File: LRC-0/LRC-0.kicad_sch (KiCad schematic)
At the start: 39 parts, among them J1 USB_C_Receptacle_USB2.0_14P, J2 Battery, SW1 SW_Push, SW2 SW_Push, U1 ESP32-C6-MINI-1, U2 SX1262IMLTRT, U3 TVS1400DRV, U4 NCP1117-3.3_SOT223, U5 TP4056-42-ESOP8, U6 BQ24075RGT

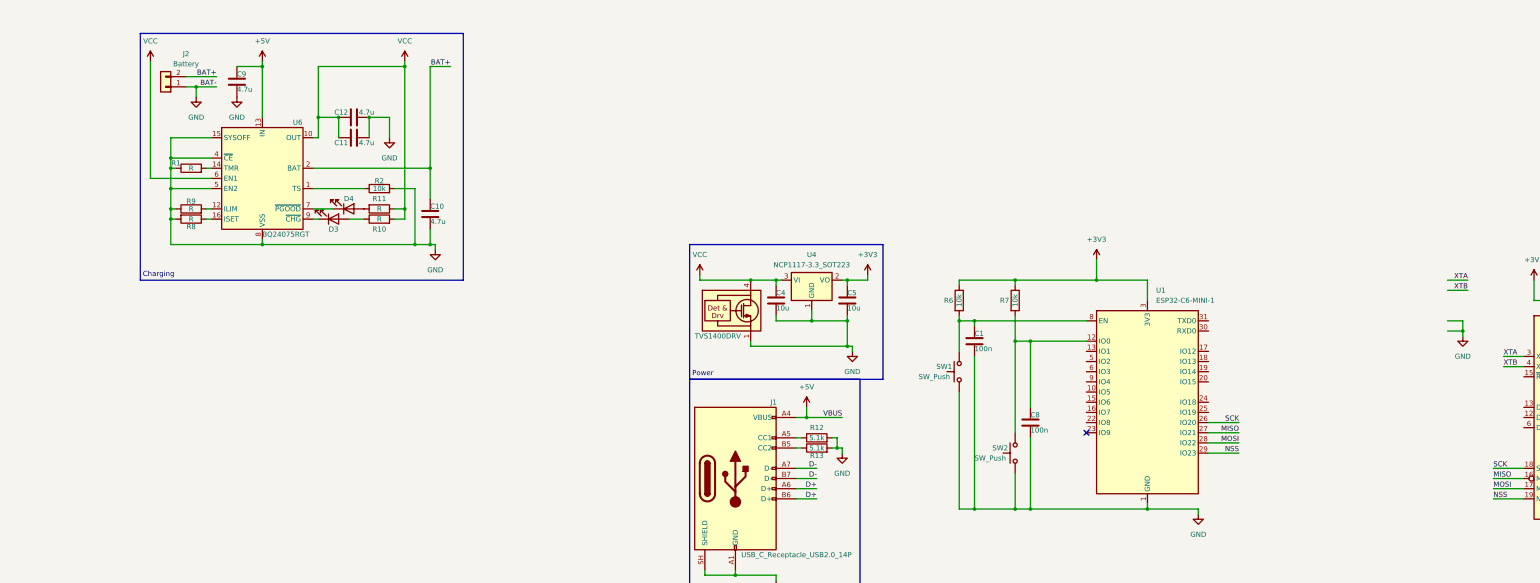
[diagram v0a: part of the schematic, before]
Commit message: footprints fixed for real
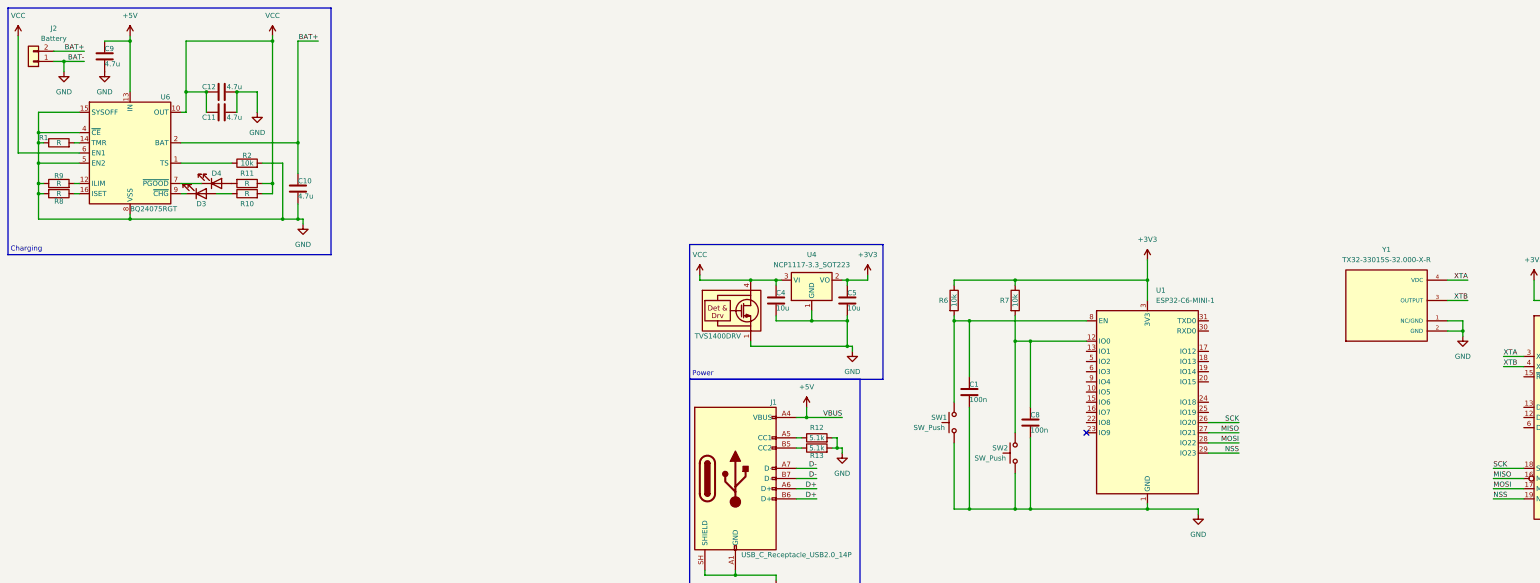
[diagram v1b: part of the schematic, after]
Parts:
- added Y1: TX32-33015S-32.000-X-R, TX32_33015S_32_000_X_R:OSC_TX32-33015S-32.000-X-R, symbol TX32_33015S_32_000_X_R:TX32-33015S-32.000-X-R
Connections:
- net GND: now also Y1.1 (NC/GND), Y1.2 (GND)
- net XTA: now also Y1.4 (VDC)
- net XTB: now also Y1.3 (OUTPUT)
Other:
- moved on the sheet: C1, C10, C11, C12, C9, D3, D4, J2, R1, R10, R11, R2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

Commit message: library dependencies fixed
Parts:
- U1: footprint RF_Module:XCVR_ESP32-C6-MINI-1U-H4 -> ESP32_C6_MINI_1U_H4:XCVR_ESP32-C6-MINI-1U-H4
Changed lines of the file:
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@@
 			)
 		)
-		(property "Footprint" "RF_Module:XCVR_ESP32-C6-MINI-1U-H4"
+		(property "Footprint" "ESP32_C6_MINI_1U_H4:XCVR_ESP32-C6-MINI-1U-H4"
 			(at 144.78 124.46 0)
 			(hide yes)

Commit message: xta fix
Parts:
- added C6: 10p, symbol Device:C
- added C7: 100n, symbol Device:C
- added L1: L, symbol Device:L
- added R14: 220, symbol Device:R
- U1: footprint ESP32_C6_MINI_1U_H4:XCVR_ESP32-C6-MINI-1U-H4 -> RF_Module:ESP32-C6-MINI-1
- Y1: footprint TX32_33015S_32_000_X_R:OSC_TX32-33015S-32.000-X-R -> TX32-33015S-32.000-X-R:OSC_TX32-33015S-32.000-X-R
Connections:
- net GND: now also C7.2
- net RFO: now also L1.1
- net XTA: now also R14.1; no longer U2.3 (XTA)
- net DIO3: now reaches U2.6 (DIO3)
- net DIO3: now also Y1.3 (OUTPUT), C7.1
- net XTB: no longer names the net of U2.4 (XTB)
- net XTB: no longer Y1.3 (OUTPUT)
- new net: C6.1, R14.2
- new net: C6.2, U2.3 (XTA)
- no-connect marks 1 -> 2
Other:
- moved on the sheet: C2, C4, C5, D1, D2, J1, R12, R13, R4, R5, U4, Y1

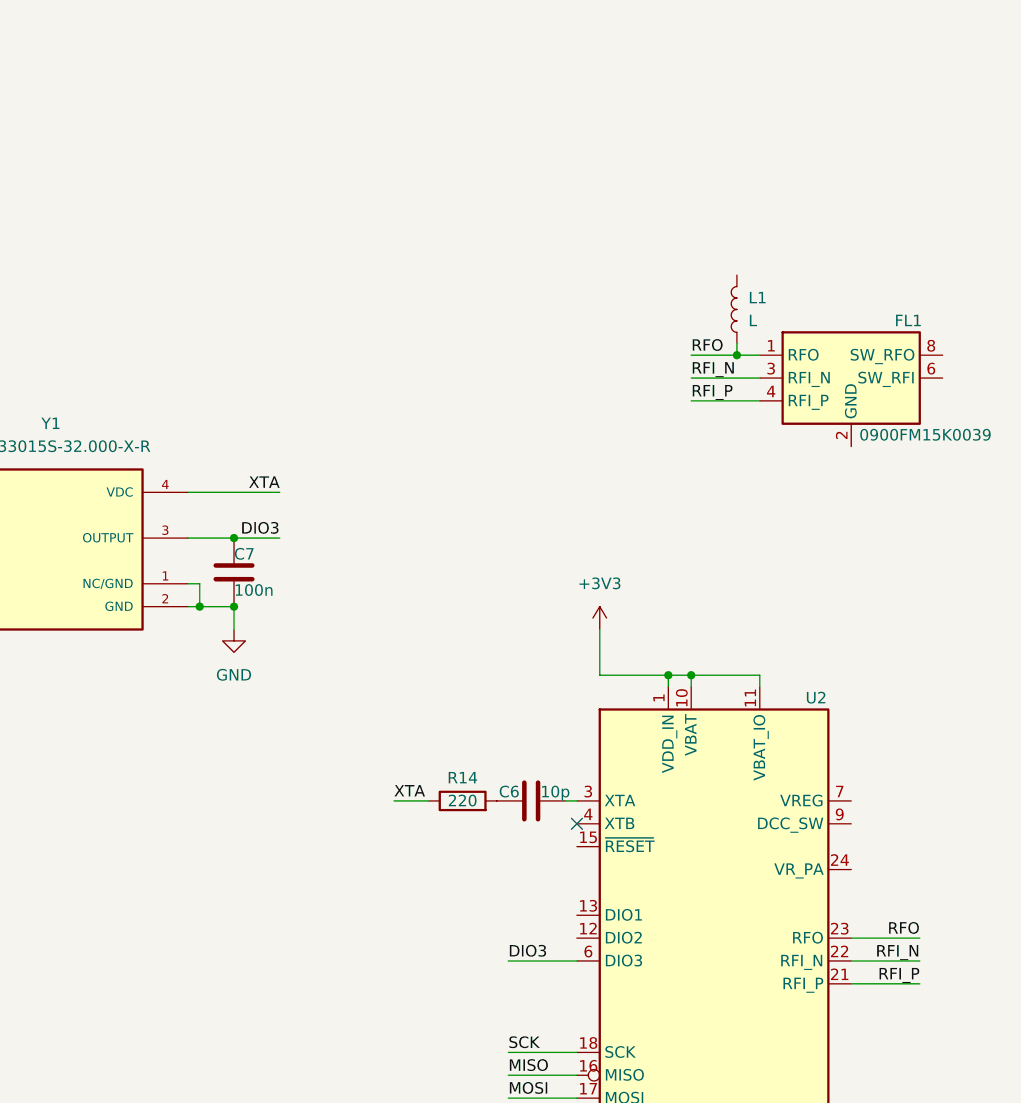
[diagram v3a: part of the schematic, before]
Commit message: schematic progress new rf switch
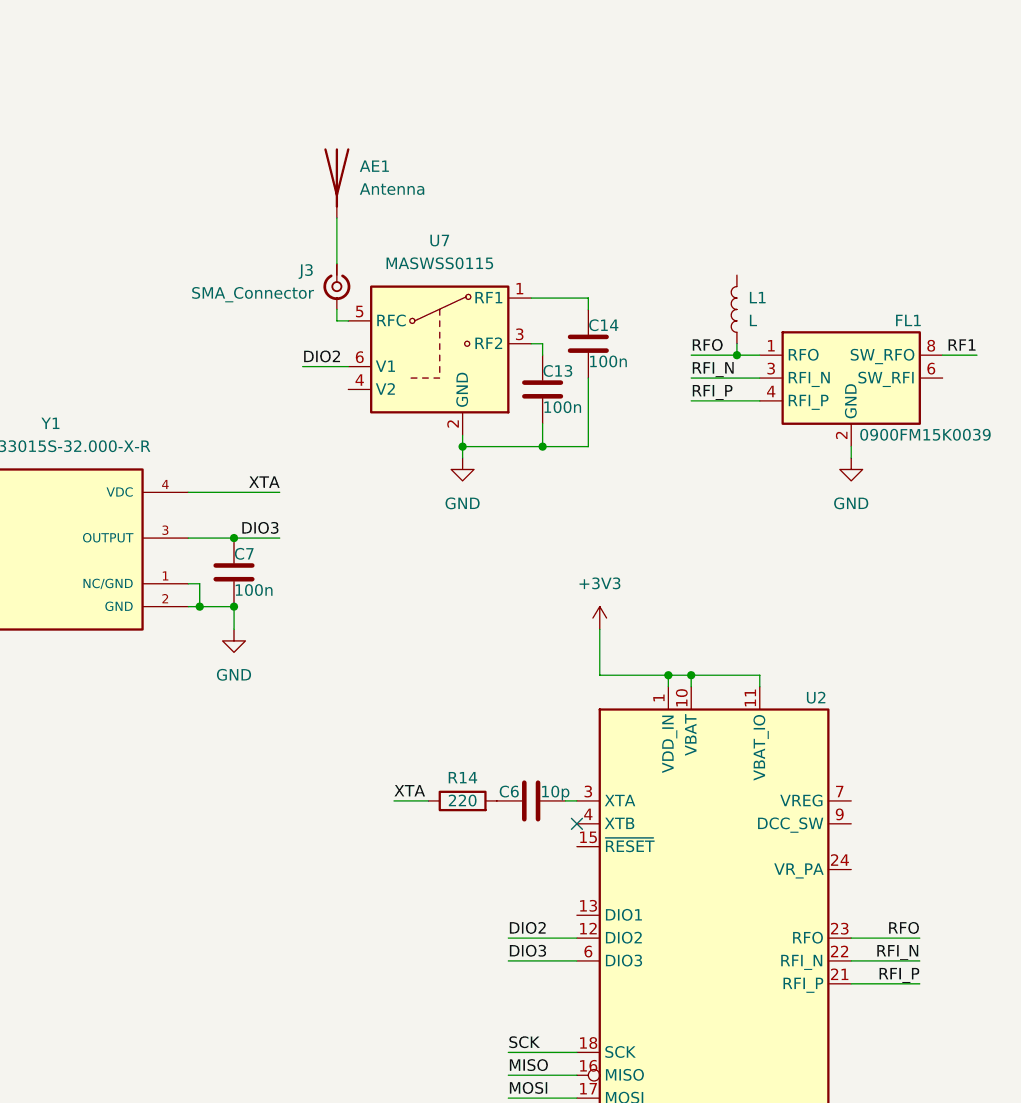
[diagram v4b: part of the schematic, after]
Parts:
- added AE1: Antenna, symbol Device:Antenna
- added C13, C14: 100n, symbol Device:C
- added J3: SMA_Connector, symbol Connector:Conn_Coaxial_Small
- added U7: MASWSS0115, Package_TO_SOT_SMD:SOT-363_SC-70-6, symbol RF_Switch:MASWSS0115
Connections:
- net GND: now also FL1.10 (GND), FL1.2 (GND), FL1.5 (GND), FL1.7 (GND), FL1.9 (GND), C13.2, C14.2, U7.2 (GND)
- net DIO2: now reaches U2.12 (DIO2)
- net DIO2: now also U7.6 (V1)
- net RF1: now reaches FL1.8 (SW_RFO)
- new net: C14.1, U7.1 (RF1)
- new net: C13.1, U7.3 (RF2)
- new net: J3.2 (Ext), U7.5 (RFC)
- new net: AE1.1 (A), J3.1 (In)

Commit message: real commit
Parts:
- added C15, C16, C17: 47n, symbol Device:C
- added L2: 15u, symbol Device:L
- C13, C14: value 100n -> 39p
- L1: value L -> 47n
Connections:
- net BAT+ is gone; now on net VCC: BT1.1 (+), C10.1, C3.1, J2.2 (Pin_2), U5.5 (BAT), U6.2 (BAT), U6.3 (BAT)
- net D+: now also U1.18 (IO13)
- net D-: now also U1.17 (IO12)
- net GND: now also C15.2, C16.2, C17.2
- net at J3.2 (Ext): no longer U7.5 (RFC)
- net PAVDD: now reaches U2.24 (VR_PA)
- net PAVDD: now also L1.2, C15.1, C16.1
- net VREG: now reaches U2.7 (VREG)
- net VREG: now also C17.1, L2.2
- net at U2.9 (DCC_SW): now also L2.1
- new net RFC: U7.5 (RFC)
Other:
- moved on the sheet: AE1, BT1, C1, C10, C11, C12, C2, C3, C4, C5, C8, C9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

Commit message: something happened
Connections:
- net RF1: now also C14.1, U7.1 (RF1)
- net RF2: now reaches C13.1, U7.3 (RF2)
- net RF2: now also FL1.6 (SW_RFI)
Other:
- moved on the sheet: C1, C14, C6, C7, C8, FL1, L1, L2, R14, R6, R7, SW1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

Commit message: commit?
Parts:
- removed AE1: Antenna, symbol Device:Antenna
- removed C15, C16, C17: 47n, symbol Device:C
- removed J3: SMA_Connector, symbol Connector:Conn_Coaxial_Small
- removed L1: 47n, symbol Device:L
- added C19: 1u, symbol Device:C
- added C20, C21: C, symbol Device:C
- L2: value 15u -> 47n
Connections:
- net PAVDD is gone; now on an unnamed net: U2.24 (VR_PA)
- net GND: now also C19.2, C20.2, C21.2
- net RFO: now also L2.2
- net NRESET: now reaches U1.24 (IO18)
- net NRESET: now also U2.15 (~{RESET})
- net DIO1: now reaches U1.25 (IO19)
- net DIO1: now also U2.13 (DIO1)
- net at L2.1: now also C20.1, C21.1; no longer U2.9 (DCC_SW)
- net VREG: no longer names the net of U2.7 (VREG)
- net VREG: now also C19.1; no longer L2.2
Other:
- note added: "CHARGING"
- note added: "IPD BALUN/FILTER"
- note added: "MCU"
- note added: "POWER"
- note added: "RF SWITCH"
- note added: "TCXO"
- note added: "TRANSCEIVER"
- note removed: "Power"
- moved on the sheet: C1, C13, C14, C6, C7, C8, FL1, R14, R6, R7, SW1, SW2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

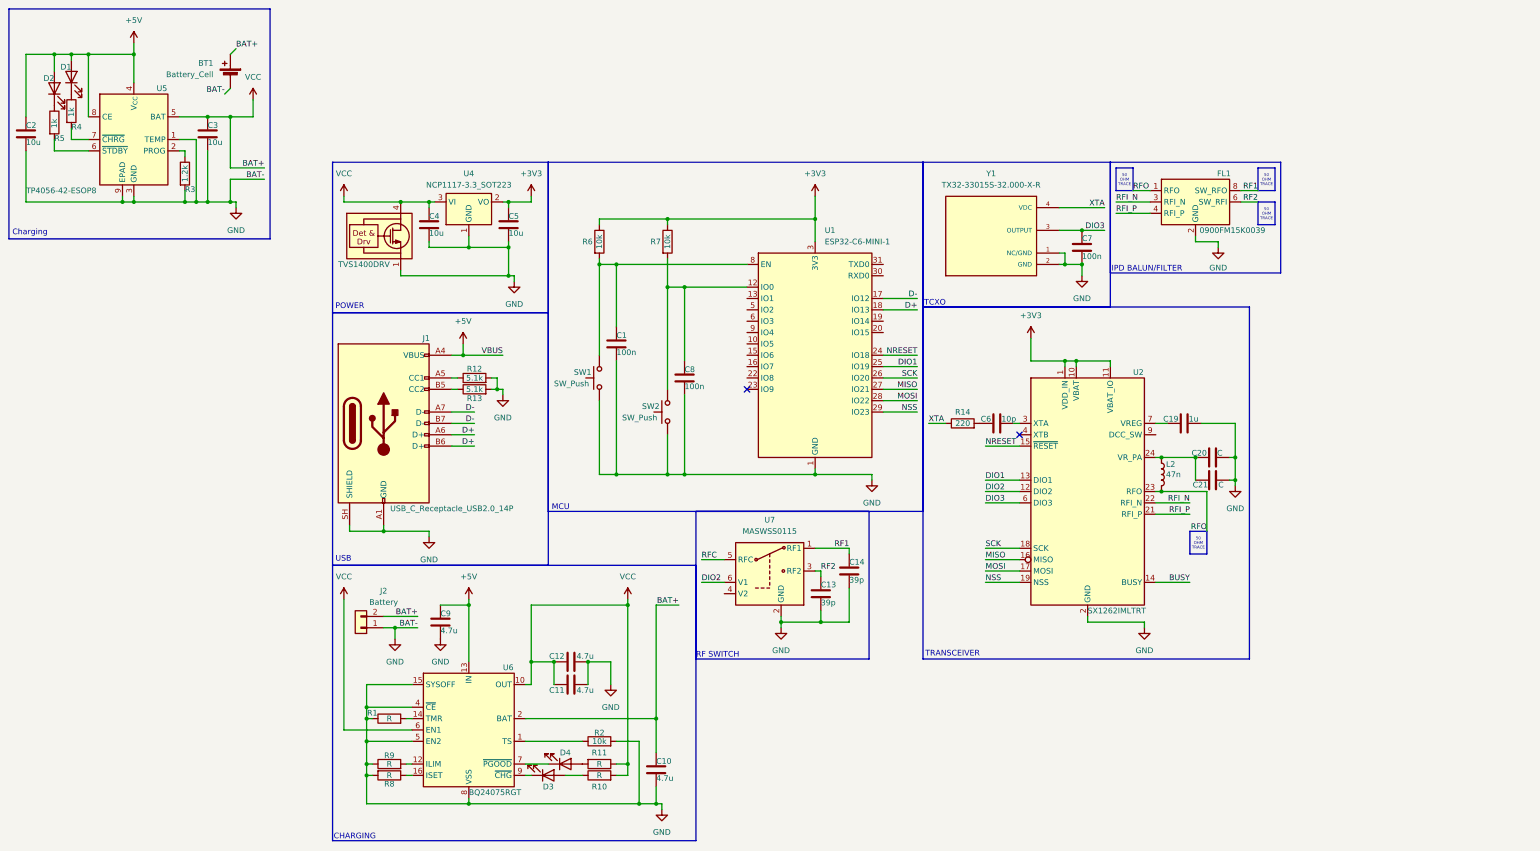
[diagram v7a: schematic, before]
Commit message: minor wiring fixes
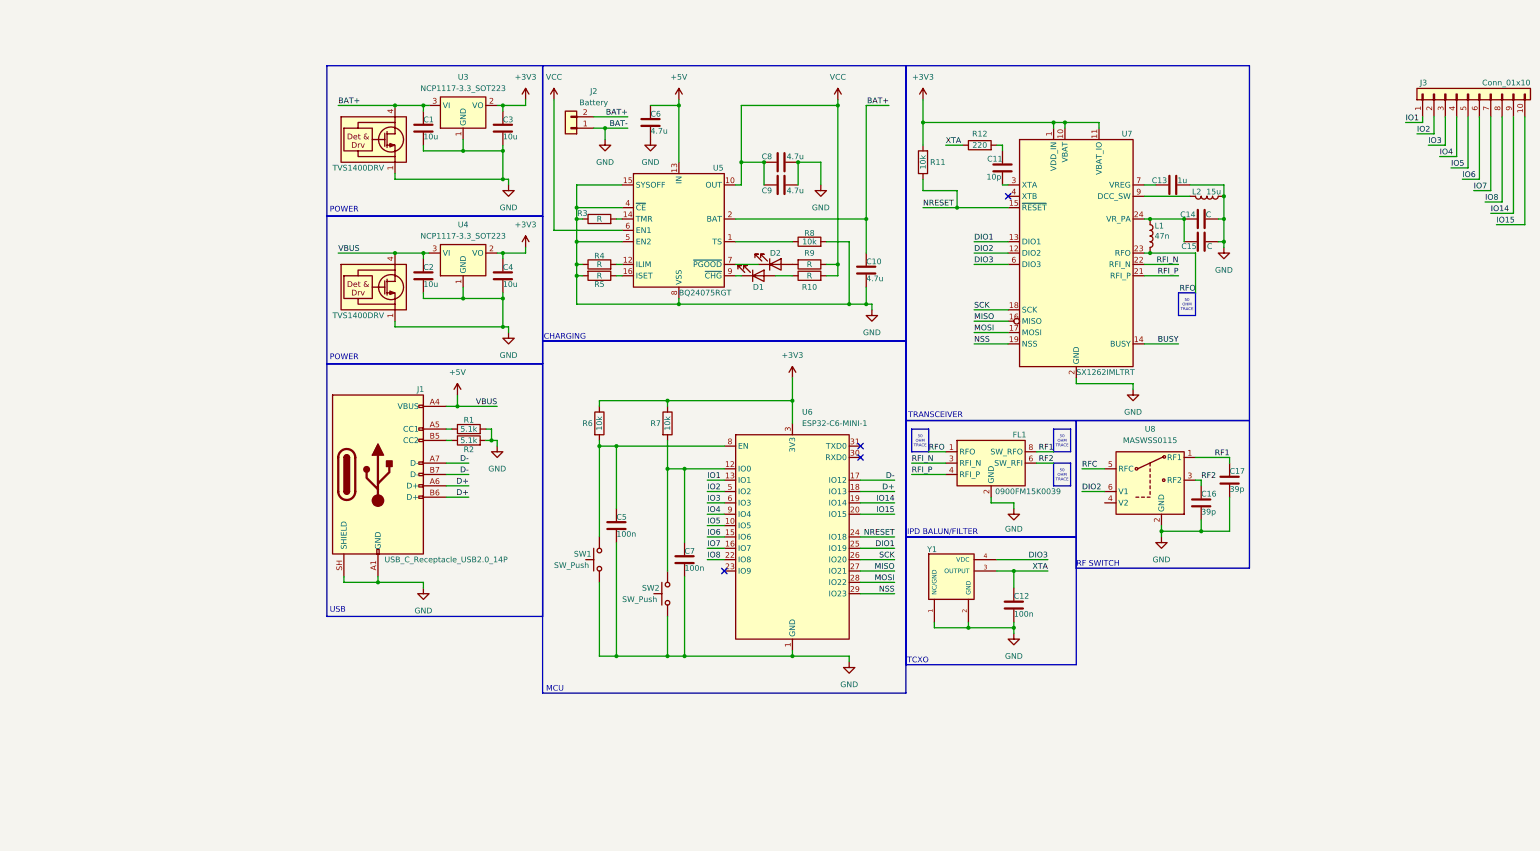
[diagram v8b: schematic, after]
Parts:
- removed BT1: Battery_Cell, symbol Device:Battery_Cell
- removed C2: 10u, symbol Device:C
- removed D1, D2: LED, symbol Device:LED
- removed R3: 1.2k, symbol Device:R
- removed R4, R5: 1k, symbol Device:R
- removed U5: TP4056-42-ESOP8, Package_SO:SOIC-8-1EP_3.9x4.9mm_P1.27mm_EP2.41x3.3mm_ThermalVias, symbol Battery_Management:TP4056-42-ESOP8
- added C1: 10u, Capacitor_SMD:C_0402_1005Metric, symbol Device:C
- added J3: Conn_01x10, symbol Connector_Generic:Conn_01x10
- added L2: 15u, symbol Device:L
- added R11: 10k, Resistor_SMD:R_0402_1005Metric, symbol Device:R
- added U1: TVS1400DRV, Package_SON:WSON-6-1EP_2x2mm_P0.65mm_EP1x1.6mm, symbol Power_Protection:TVS1400DRV
- added U3: NCP1117-3.3_SOT223, Package_TO_SOT_SMD:SOT-223-3_TabPin2, symbol Regulator_Linear:NCP1117-3.3_SOT223
- C10, C3: footprint (none) -> Capacitor_SMD:C_0402_1005Metric
- C11: renamed from C6; footprint (none) -> Capacitor_SMD:C_0402_1005Metric
- C12: renamed from C7; footprint (none) -> Capacitor_SMD:C_0402_1005Metric
- C13: renamed from C19; footprint (none) -> Capacitor_SMD:C_0402_1005Metric
- C14: renamed from C20; footprint (none) -> Capacitor_SMD:C_0402_1005Metric
- C15: renamed from C21; footprint (none) -> Capacitor_SMD:C_0402_1005Metric
- C16: renamed from C13; footprint (none) -> Capacitor_SMD:C_0402_1005Metric
- C17: renamed from C14; footprint (none) -> Capacitor_SMD:C_0402_1005Metric
- C2: renamed from C4; footprint (none) -> Capacitor_SMD:C_0402_1005Metric
- C4: renamed from C5; footprint (none) -> Capacitor_SMD:C_0402_1005Metric
- C5: renamed from C1; footprint (none) -> Capacitor_SMD:C_0402_1005Metric
- C6: renamed from C9; footprint (none) -> Capacitor_SMD:C_0402_1005Metric
- C7: renamed from C8; footprint (none) -> Capacitor_SMD:C_0402_1005Metric
- C8: renamed from C12; footprint (none) -> Capacitor_SMD:C_0402_1005Metric
- C9: renamed from C11; footprint (none) -> Capacitor_SMD:C_0402_1005Metric
- R1: renamed from R12; footprint (none) -> Resistor_SMD:R_0402_1005Metric
- R10, R6, R7: footprint (none) -> Resistor_SMD:R_0402_1005Metric
- R12: renamed from R14; footprint (none) -> Resistor_SMD:R_0402_1005Metric
- R2: renamed from R13; footprint (none) -> Resistor_SMD:R_0402_1005Metric
- R3: renamed from R1; footprint (none) -> Resistor_SMD:R_0402_1005Metric
- R4: renamed from R9; footprint (none) -> Resistor_SMD:R_0402_1005Metric
- R5: renamed from R8; footprint (none) -> Resistor_SMD:R_0402_1005Metric
- R8: renamed from R2; footprint (none) -> Resistor_SMD:R_0402_1005Metric
- R9: renamed from R11; footprint (none) -> Resistor_SMD:R_0402_1005Metric
- Y1: footprint TX32-33015S-32.000-X-R:OSC_TX32-33015S-32.000-X-R -> TX32_33015S_32_000_X_R:OSC_TX32-33015S-32.000-X-R
- renumbered D3 to D1, D4 to D2, L2 to L1, U3 to U2, U6 to U5, U1 to U6, U2 to U7, U7 to U8
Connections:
- net +3V3: now also C3.1, R11.2, U3.2 (VO)
- net +5V: now also C2.1, U2.4 (IN), U2.5 (IN), U2.6 (IN), U4.3 (VI)
- net DIO3: now also Y1.4 (VDC); no longer C12.1, Y1.3 (OUTPUT)
- net GND: now also C1.2, L2.1, U1.1 (GND), U1.2 (GND), U1.3 (GND), U1.7 (GND), U3.1 (GND)
- net NRESET: now also R11.1
- net VCC: no longer C10.1, C2.1, C3.1, J2.2 (Pin_2), U2.4 (IN), U2.5 (IN), U2.6 (IN), U4.3 (VI), U5.2 (BAT), U5.3 (BAT)
- net XTA: now also C12.1, Y1.3 (OUTPUT); no longer Y1.4 (VDC)
- net IO5: now reaches U6.10 (IO5)
- net IO5: now also J3.5 (Pin_5)
- net IO1: now reaches U6.13 (IO1)
- net IO1: now also J3.1 (Pin_1)
- net IO6: now reaches U6.15 (IO6)
- net IO6: now also J3.6 (Pin_6)
- net IO7: now reaches U6.16 (IO7)
- net IO7: now also J3.7 (Pin_7)
- net IO14: now reaches U6.19 (IO14)
- net IO14: now also J3.9 (Pin_9)
- net IO15: now reaches U6.20 (IO15)
- net IO15: now also J3.10 (Pin_10)
- net IO8: now reaches U6.22 (IO8)
- net IO8: now also J3.8 (Pin_8)
- net IO2: now reaches U6.5 (IO2)
- net IO2: now also J3.2 (Pin_2)
- net IO3: now reaches U6.6 (IO3)
- net IO3: now also J3.3 (Pin_3)
- net IO4: now reaches U6.9 (IO4)
- net IO4: now also J3.4 (Pin_4)
- net at C11.1: now also U7.3 (XTA); no longer R12.2
- net at C11.2: now also R12.2; no longer U7.3 (XTA)
- net at U7.9 (DCC_SW): now also L2.2
- new net BAT+: C1.1, C10.1, J2.2 (Pin_2), U1.4 (IN), U1.5 (IN), U1.6 (IN), U3.3 (VI), U5.2 (BAT), U5.3 (BAT)
- no-connect marks 2 -> 4
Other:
- note removed: "Charging"
- moved on the sheet: C10, C11, C12, C13, C14, C15, C16, C17, C2, C4, C5, C6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
